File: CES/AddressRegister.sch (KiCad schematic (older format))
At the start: 8 parts

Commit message: Adding 74HC versions of 74LS chips
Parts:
- removed U?: RE1, symbol 74xx:74LS173
- removed U?: RE2, symbol 74xx:74LS173
- removed U?: RE3, symbol 74xx:74LS173
- removed U?: RE4, symbol 74xx:74LS173
- added U?: RE1, symbol CES:74HC173
- added U?: RE2, symbol CES:74HC173
- added U?: RE3, symbol CES:74HC173
- added U?: RE4, symbol CES:74HC173
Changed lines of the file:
@@
 Comment4 ""
 $EndDescr
-$Comp
-L 74xx:74LS173 U?
-U 1 1 61BF820F
-P 4050 1750
-F 0 "U?" H 4300 2500 50  0000 C CNN
-F 1 "RE1" H 4050 1750 50  0000 C CNN
-F 2 "" H 4050 1750 50  0001 C CNN
-F 3 "http://www.ti.com/lit/gpn/sn74LS173" H 4050 1750 50  0001 C CNN
-	1    4050 1750
-	1    0    0    -1
-$EndComp
-$Comp
-L 74xx:74LS173 U?
-U 1 1 61BF8215
-P 4050 4100
-F 0 "U?" H 4300 4850 50  0000 C CNN
-F 1 "RE2" H 4050 4100 50  0000 C CNN
-F 2 "" H 4050 4100 50  0001 C CNN
-F 3 "http://www.ti.com/lit/gpn/sn74LS173" H 4050 4100 50  0001 C CNN
-	1    4050 4100
-	1    0    0    -1
-$EndComp
-$Comp
-L 74xx:74LS173 U?
-U 1 1 61BF821B
-P 4050 6450
-F 0 "U?" H 4300 7200 50  0000 C CNN
-F 1 "RE3" H 4050 6450 50  0000 C CNN
-F 2 "" H 4050 6450 50  0001 C CNN
-F 3 "http://www.ti.com/lit/gpn/sn74LS173" H 4050 6450 50  0001 C CNN
-	1    4050 6450
-	1    0    0    -1
-$EndComp
-$Comp
-L 74xx:74LS173 U?
-U 1 1 61BF8221
-P 4050 8800
-F 0 "U?" H 4300 9600 50  0000 C CNN
-F 1 "RE4" H 4050 8800 50  0000 C CNN
-F 2 "" H 4050 8800 50  0001 C CNN
-F 3 "http://www.ti.com/lit/gpn/sn74LS173" H 4050 8800 50  0001 C CNN
-	1    4050 8800
-	1    0    0    -1
-$EndComp
 Wire Wire Line
 	4550 1150 5750 1150
@@
 Wire Wire Line
 	1900 10350 1750 10350
+$Comp
+L CES:74HC173 U?
+U 1 1 60900C75
+P 4050 1750
+F 0 "U?" H 4050 2831 50  0000 C CNN
+F 1 "RE1" H 4050 1750 50  0000 C CNN
+F 2 "" H 4050 1750 50  0001 C CNN
+F 3 "http://www.ti.com/lit/gpn/cd74HC173" H 4050 1750 50  0001 C CNN
+	1    4050 1750
+	1    0    0    -1
+$EndComp
+$Comp
+L CES:74HC173 U?
+U 1 1 60901D89
+P 4050 4100
+F 0 "U?" H 4050 5181 50  0000 C CNN
+F 1 "RE2" H 4050 4100 50  0000 C CNN
+F 2 "" H 4050 4100 50  0001 C CNN
+F 3 "http://www.ti.com/lit/gpn/cd74HC173" H 4050 4100 50  0001 C CNN
+	1    4050 4100
+	1    0    0    -1
+$EndComp
+$Comp
+L CES:74HC173 U?
+U 1 1 609029C7
+P 4050 6450
+F 0 "U?" H 4050 7531 50  0000 C CNN
+F 1 "RE3" H 4050 6450 50  0000 C CNN
+F 2 "" H 4050 6450 50  0001 C CNN
+F 3 "http://www.ti.com/lit/gpn/cd74HC173" H 4050 6450 50  0001 C CNN
+	1    4050 6450
+	1    0    0    -1
+$EndComp
+$Comp
+L CES:74HC173 U?
+U 1 1 609031EB
+P 4050 8800
+F 0 "U?" H 4050 9881 50  0000 C CNN
+F 1 "RE4" H 4050 8800 50  0000 C CNN
+F 2 "" H 4050 8800 50  0001 C CNN
+F 3 "http://www.ti.com/lit/gpn/cd74HC173" H 4050 8800 50  0001 C CNN
+	1    4050 8800
+	1    0    0    -1
+$EndComp
 $EndSCHEMATC

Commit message: Control Unit
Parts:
- gave numbers to parts that had none: 8
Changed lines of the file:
@@
 $Descr A4 8268 11693 portrait
 encoding utf-8
-Sheet 7 16
+Sheet 7 17
 Title "CES"
 Date "2021-04-24"
@@
 VEB13
 $Comp
-L power:GND #PWR?
+L power:GND #PWR0714
 U 1 1 60A1EDC1
 P 4050 9700
-F 0 "#PWR?" H 4050 9450 50  0001 C CNN
+F 0 "#PWR0714" H 4050 9450 50  0001 C CNN
 F 1 "GND" H 4055 9527 50  0000 C CNN
 F 2 "" H 4050 9700 50  0001 C CNN
@@
 $EndComp
 $Comp
-L power:GND #PWR?
+L power:GND #PWR0712
 U 1 1 60A1F39E
 P 4050 7350
-F 0 "#PWR?" H 4050 7100 50  0001 C CNN
+F 0 "#PWR0712" H 4050 7100 50  0001 C CNN
 F 1 "GND" H 4055 7177 50  0000 C CNN
 F 2 "" H 4050 7350 50  0001 C CNN
@@
 $EndComp
 $Comp
-L power:GND #PWR?
+L power:GND #PWR0710
 U 1 1 60A1F890
 P 4050 5000
-F 0 "#PWR?" H 4050 4750 50  0001 C CNN
+F 0 "#PWR0710" H 4050 4750 50  0001 C CNN
 F 1 "GND" H 4055 4827 50  0000 C CNN
 F 2 "" H 4050 5000 50  0001 C CNN
@@
 $EndComp
 $Comp
-L power:GND #PWR?
+L power:GND #PWR0708
 U 1 1 60A1FDC0
 P 4050 2650
-F 0 "#PWR?" H 4050 2400 50  0001 C CNN
+F 0 "#PWR0708" H 4050 2400 50  0001 C CNN
 F 1 "GND" H 4055 2477 50  0000 C CNN
 F 2 "" H 4050 2650 50  0001 C CNN
@@
 $EndComp
 $Comp
-L power:VCC #PWR?
+L power:VCC #PWR0707
 U 1 1 60A20410
 P 4050 850
-F 0 "#PWR?" H 4050 700 50  0001 C CNN
+F 0 "#PWR0707" H 4050 700 50  0001 C CNN
 F 1 "VCC" H 4065 1023 50  0000 C CNN
 F 2 "" H 4050 850 50  0001 C CNN
@@
 $EndComp
 $Comp
-L power:VCC #PWR?
+L power:VCC #PWR0709
 U 1 1 60A20A35
 P 4050 3200
-F 0 "#PWR?" H 4050 3050 50  0001 C CNN
+F 0 "#PWR0709" H 4050 3050 50  0001 C CNN
 F 1 "VCC" H 4065 3373 50  0000 C CNN
 F 2 "" H 4050 3200 50  0001 C CNN
@@
 $EndComp
 $Comp
-L power:VCC #PWR?
+L power:VCC #PWR0711
 U 1 1 60A20DA9
 P 4050 5550
-F 0 "#PWR?" H 4050 5400 50  0001 C CNN
+F 0 "#PWR0711" H 4050 5400 50  0001 C CNN
 F 1 "VCC" H 4065 5723 50  0000 C CNN
 F 2 "" H 4050 5550 50  0001 C CNN
@@
 $EndComp
 $Comp
-L power:VCC #PWR?
+L power:VCC #PWR0713
 U 1 1 60A2119F
 P 4050 7900
-F 0 "#PWR?" H 4050 7750 50  0001 C CNN
+F 0 "#PWR0713" H 4050 7750 50  0001 C CNN
 F 1 "VCC" H 4065 8073 50  0000 C CNN
 F 2 "" H 4050 7900 50  0001 C CNN
@@
 Connection ~ 3350 6650
 $Comp
-L power:GND #PWR?
+L power:GND #PWR0705
 U 1 1 60A6C19B
 P 3350 7150
-F 0 "#PWR?" H 3350 6900 50  0001 C CNN
+F 0 "#PWR0705" H 3350 6900 50  0001 C CNN
 F 1 "GND" H 3355 6977 50  0000 C CNN
 F 2 "" H 3350 7150 50  0001 C CNN
@@
 Connection ~ 3350 9000
 $Comp
-L power:GND #PWR?
+L power:GND #PWR0706
 U 1 1 60A6D091
 P 3350 9500
-F 0 "#PWR?" H 3350 9250 50  0001 C CNN
+F 0 "#PWR0706" H 3350 9250 50  0001 C CNN
 F 1 "GND" H 3355 9327 50  0000 C CNN
 F 2 "" H 3350 9500 50  0001 C CNN
@@
 Connection ~ 3350 4300
 $Comp
-L power:GND #PWR?
+L power:GND #PWR0704
 U 1 1 60A6E8ED
 P 3350 4800
-F 0 "#PWR?" H 3350 4550 50  0001 C CNN
+F 0 "#PWR0704" H 3350 4550 50  0001 C CNN
 F 1 "GND" H 3355 4627 50  0000 C CNN
 F 2 "" H 3350 4800 50  0001 C CNN
@@
 Connection ~ 3350 1950
 $Comp
-L power:GND #PWR?
+L power:GND #PWR0703
 U 1 1 60A6F961
 P 3350 2450
-F 0 "#PWR?" H 3350 2200 50  0001 C CNN
+F 0 "#PWR0703" H 3350 2200 50  0001 C CNN
 F 1 "GND" H 3355 2277 50  0000 C CNN
 F 2 "" H 3350 2450 50  0001 C CNN
@@
 	2350 8300 3550 8300
 $Comp
-L Device:C C?
+L Device:C C701
 U 1 1 60A83BCD
 P 1450 10600
-F 0 "C?" H 1500 10700 50  0000 L CNN
+F 0 "C701" H 1500 10700 50  0000 L CNN
 F 1 "100nF" H 1500 10500 50  0000 L CNN
 F 2 "" H 1488 10450 50  0001 C CNN
@@
 $EndComp
 $Comp
-L Device:C C?
+L Device:C C702
 U 1 1 60A83BD3
 P 1750 10600
-F 0 "C?" H 1800 10700 50  0000 L CNN
+F 0 "C702" H 1800 10700 50  0000 L CNN
 F 1 "100nF" H 1800 10500 50  0000 L CNN
 F 2 "" H 1788 10450 50  0001 C CNN
@@
 $EndComp
 $Comp
-L Device:C C?
+L Device:C C703
 U 1 1 60A83BD9
 P 2050 10600
-F 0 "C?" H 2100 10700 50  0000 L CNN
+F 0 "C703" H 2100 10700 50  0000 L CNN
 F 1 "100nF" H 2100 10500 50  0000 L CNN
 F 2 "" H 2088 10450 50  0001 C CNN
@@
 $EndComp
 $Comp
-L Device:C C?
+L Device:C C704
 U 1 1 60A83BDF
 P 2350 10600
-F 0 "C?" H 2400 10700 50  0000 L CNN
+F 0 "C704" H 2400 10700 50  0000 L CNN
 F 1 "100nF" H 2400 10500 50  0000 L CNN
 F 2 "" H 2388 10450 50  0001 C CNN
@@
 	1750 10850 1900 10850
 $Comp
-L power:GND #PWR?
+L power:GND #PWR0702
 U 1 1 60A83BF7
 P 1900 10850
-F 0 "#PWR?" H 1900 10600 50  0001 C CNN
+F 0 "#PWR0702" H 1900 10600 50  0001 C CNN
 F 1 "GND" H 1905 10677 50  0000 C CNN
 F 2 "" H 1900 10850 50  0001 C CNN
@@
 	1900 10850 2050 10850
 $Comp
-L power:VCC #PWR?
+L power:VCC #PWR0701
 U 1 1 60A83BFF
 P 1900 10350
-F 0 "#PWR?" H 1900 10200 50  0001 C CNN
+F 0 "#PWR0701" H 1900 10200 50  0001 C CNN
 F 1 "VCC" H 1915 10523 50  0000 C CNN
 F 2 "" H 1900 10350 50  0001 C CNN
@@
 	1900 10350 1750 10350
 $Comp
-L CES:74HC173 U?
+L CES:74HC173 U701
 U 1 1 60900C75
 P 4050 1750
-F 0 "U?" H 4050 2831 50  0000 C CNN
+F 0 "U701" H 4050 2831 50  0000 C CNN
 F 1 "RE1" H 4050 1750 50  0000 C CNN
 F 2 "" H 4050 1750 50  0001 C CNN
@@
 $EndComp
 $Comp
-L CES:74HC173 U?
+L CES:74HC173 U702
 U 1 1 60901D89
 P 4050 4100
-F 0 "U?" H 4050 5181 50  0000 C CNN
+F 0 "U702" H 4050 5181 50  0000 C CNN
 F 1 "RE2" H 4050 4100 50  0000 C CNN
 F 2 "" H 4050 4100 50  0001 C CNN
@@
 $EndComp
 $Comp
-L CES:74HC173 U?
+L CES:74HC173 U703
 U 1 1 609029C7
 P 4050 6450
-F 0 "U?" H 4050 7531 50  0000 C CNN
+F 0 "U703" H 4050 7531 50  0000 C CNN
 F 1 "RE3" H 4050 6450 50  0000 C CNN
 F 2 "" H 4050 6450 50  0001 C CNN
@@
 $EndComp
 $Comp
-L CES:74HC173 U?
+L CES:74HC173 U704
 U 1 1 609031EB
 P 4050 8800
-F 0 "U?" H 4050 9881 50  0000 C CNN
+F 0 "U704" H 4050 9881 50  0000 C CNN
 F 1 "RE4" H 4050 8800 50  0000 C CNN
 F 2 "" H 4050 8800 50  0001 C CNN

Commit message: Assigning footprints and generating netlist
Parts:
- C701, C702, C703, C704: footprint (none) -> Capacitor_THT:CP_Radial_D5.0mm_P2.50mm
- U701, U702, U703, U704: footprint (none) -> Package_DIP:DIP-16_W7.62mm
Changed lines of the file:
@@
 F 0 "C701" H 1500 10700 50  0000 L CNN
 F 1 "100nF" H 1500 10500 50  0000 L CNN
-F 2 "" H 1488 10450 50  0001 C CNN
+F 2 "Capacitor_THT:CP_Radial_D5.0mm_P2.50mm" H 1488 10450 50  0001 C CNN
 F 3 "~" H 1450 10600 50  0001 C CNN
 	1    1450 10600
@@
 F 0 "C702" H 1800 10700 50  0000 L CNN
 F 1 "100nF" H 1800 10500 50  0000 L CNN
-F 2 "" H 1788 10450 50  0001 C CNN
+F 2 "Capacitor_THT:CP_Radial_D5.0mm_P2.50mm" H 1788 10450 50  0001 C CNN
 F 3 "~" H 1750 10600 50  0001 C CNN
 	1    1750 10600
@@
 F 0 "C703" H 2100 10700 50  0000 L CNN
 F 1 "100nF" H 2100 10500 50  0000 L CNN
-F 2 "" H 2088 10450 50  0001 C CNN
+F 2 "Capacitor_THT:CP_Radial_D5.0mm_P2.50mm" H 2088 10450 50  0001 C CNN
 F 3 "~" H 2050 10600 50  0001 C CNN
 	1    2050 10600
@@
 F 0 "C704" H 2400 10700 50  0000 L CNN
 F 1 "100nF" H 2400 10500 50  0000 L CNN
-F 2 "" H 2388 10450 50  0001 C CNN
+F 2 "Capacitor_THT:CP_Radial_D5.0mm_P2.50mm" H 2388 10450 50  0001 C CNN
 F 3 "~" H 2350 10600 50  0001 C CNN
 	1    2350 10600
@@
 F 0 "U701" H 4050 2831 50  0000 C CNN
 F 1 "RE1" H 4050 1750 50  0000 C CNN
-F 2 "" H 4050 1750 50  0001 C CNN
+F 2 "Package_DIP:DIP-16_W7.62mm" H 4050 1750 50  0001 C CNN
 F 3 "http://www.ti.com/lit/gpn/cd74HC173" H 4050 1750 50  0001 C CNN
 	1    4050 1750
@@
 F 0 "U702" H 4050 5181 50  0000 C CNN
 F 1 "RE2" H 4050 4100 50  0000 C CNN
-F 2 "" H 4050 4100 50  0001 C CNN
+F 2 "Package_DIP:DIP-16_W7.62mm" H 4050 4100 50  0001 C CNN
 F 3 "http://www.ti.com/lit/gpn/cd74HC173" H 4050 4100 50  0001 C CNN
 	1    4050 4100
@@
 F 0 "U703" H 4050 7531 50  0000 C CNN
 F 1 "RE3" H 4050 6450 50  0000 C CNN
-F 2 "" H 4050 6450 50  0001 C CNN
+F 2 "Package_DIP:DIP-16_W7.62mm" H 4050 6450 50  0001 C CNN
 F 3 "http://www.ti.com/lit/gpn/cd74HC173" H 4050 6450 50  0001 C CNN
 	1    4050 6450
@@
 F 0 "U704" H 4050 9881 50  0000 C CNN
 F 1 "RE4" H 4050 8800 50  0000 C CNN
-F 2 "" H 4050 8800 50  0001 C CNN
+F 2 "Package_DIP:DIP-16_W7.62mm" H 4050 8800 50  0001 C CNN
 F 3 "http://www.ti.com/lit/gpn/cd74HC173" H 4050 8800 50  0001 C CNN
 	1    4050 8800

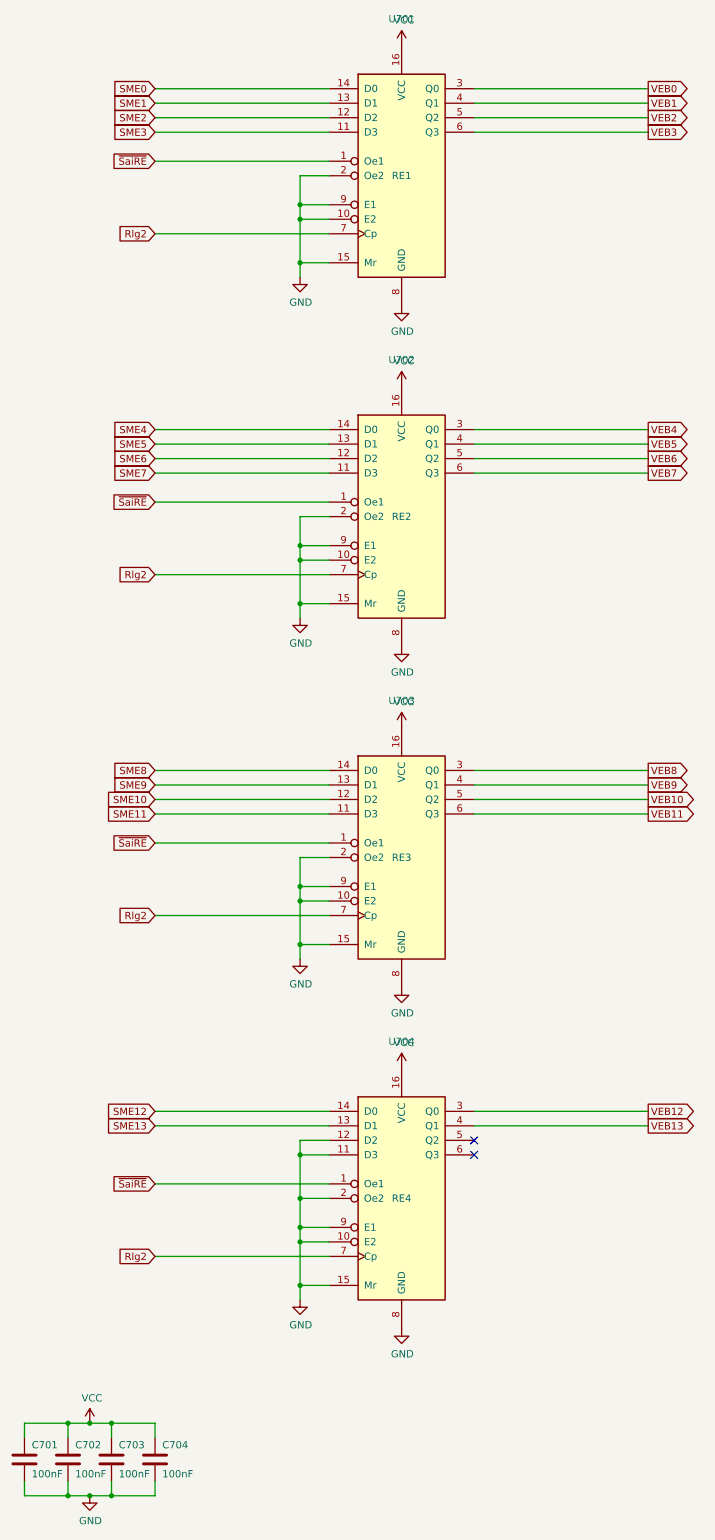
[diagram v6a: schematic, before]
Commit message: Correcting footprints errors
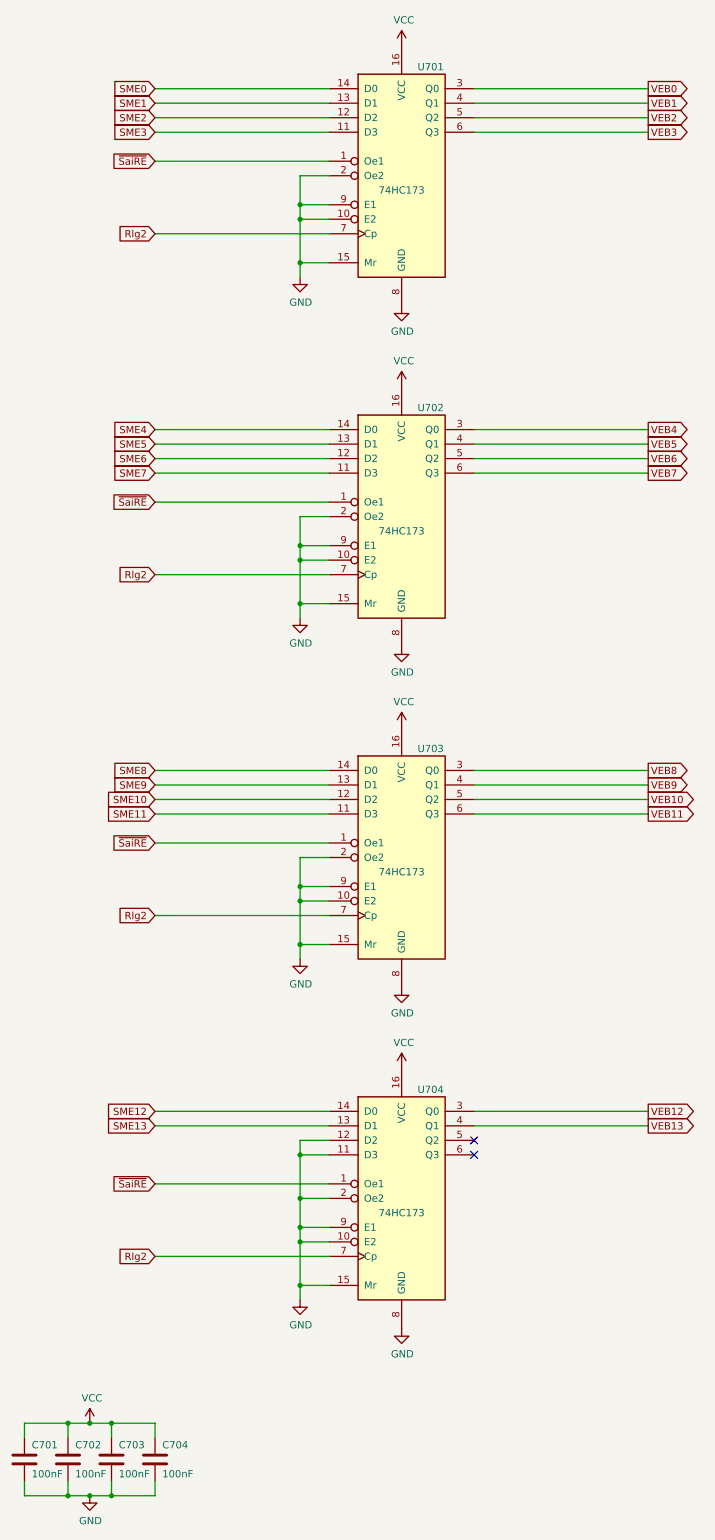
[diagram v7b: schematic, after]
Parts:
- C701, C702, C703, C704: footprint Capacitor_THT:CP_Radial_D5.0mm_P2.50mm -> Capacitor_THT:C_Disc_D4.3mm_W1.9mm_P5.00mm
- U701: value RE1 -> 74HC173
- U702: value RE2 -> 74HC173
- U703: value RE3 -> 74HC173
- U704: value RE4 -> 74HC173
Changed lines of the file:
@@
 F 0 "C701" H 1500 10700 50  0000 L CNN
 F 1 "100nF" H 1500 10500 50  0000 L CNN
-F 2 "Capacitor_THT:CP_Radial_D5.0mm_P2.50mm" H 1488 10450 50  0001 C CNN
+F 2 "Capacitor_THT:C_Disc_D4.3mm_W1.9mm_P5.00mm" H 1488 10450 50  0001 C CNN
 F 3 "~" H 1450 10600 50  0001 C CNN
 	1    1450 10600
@@
 F 0 "C702" H 1800 10700 50  0000 L CNN
 F 1 "100nF" H 1800 10500 50  0000 L CNN
-F 2 "Capacitor_THT:CP_Radial_D5.0mm_P2.50mm" H 1788 10450 50  0001 C CNN
+F 2 "Capacitor_THT:C_Disc_D4.3mm_W1.9mm_P5.00mm" H 1788 10450 50  0001 C CNN
 F 3 "~" H 1750 10600 50  0001 C CNN
 	1    1750 10600
@@
 F 0 "C703" H 2100 10700 50  0000 L CNN
 F 1 "100nF" H 2100 10500 50  0000 L CNN
-F 2 "Capacitor_THT:CP_Radial_D5.0mm_P2.50mm" H 2088 10450 50  0001 C CNN
+F 2 "Capacitor_THT:C_Disc_D4.3mm_W1.9mm_P5.00mm" H 2088 10450 50  0001 C CNN
 F 3 "~" H 2050 10600 50  0001 C CNN
 	1    2050 10600
@@
 F 0 "C704" H 2400 10700 50  0000 L CNN
 F 1 "100nF" H 2400 10500 50  0000 L CNN
-F 2 "Capacitor_THT:CP_Radial_D5.0mm_P2.50mm" H 2388 10450 50  0001 C CNN
+F 2 "Capacitor_THT:C_Disc_D4.3mm_W1.9mm_P5.00mm" H 2388 10450 50  0001 C CNN
 F 3 "~" H 2350 10600 50  0001 C CNN
 	1    2350 10600
@@
 U 1 1 60900C75
 P 4050 1750
-F 0 "U701" H 4050 2831 50  0000 C CNN
-F 1 "RE1" H 4050 1750 50  0000 C CNN
+F 0 "U701" H 4250 2500 50  0000 C CNN
+F 1 "74HC173" H 4050 1650 50  0000 C CNN
 F 2 "Package_DIP:DIP-16_W7.62mm" H 4050 1750 50  0001 C CNN
 F 3 "http://www.ti.com/lit/gpn/cd74HC173" H 4050 1750 50  0001 C CNN
@@
 U 1 1 60901D89
 P 4050 4100
-F 0 "U702" H 4050 5181 50  0000 C CNN
-F 1 "RE2" H 4050 4100 50  0000 C CNN
+F 0 "U702" H 4250 4850 50  0000 C CNN
+F 1 "74HC173" H 4050 4000 50  0000 C CNN
 F 2 "Package_DIP:DIP-16_W7.62mm" H 4050 4100 50  0001 C CNN
 F 3 "http://www.ti.com/lit/gpn/cd74HC173" H 4050 4100 50  0001 C CNN
@@
 U 1 1 609029C7
 P 4050 6450
-F 0 "U703" H 4050 7531 50  0000 C CNN
-F 1 "RE3" H 4050 6450 50  0000 C CNN
+F 0 "U703" H 4250 7200 50  0000 C CNN
+F 1 "74HC173" H 4050 6350 50  0000 C CNN
 F 2 "Package_DIP:DIP-16_W7.62mm" H 4050 6450 50  0001 C CNN
 F 3 "http://www.ti.com/lit/gpn/cd74HC173" H 4050 6450 50  0001 C CNN
@@
 U 1 1 609031EB
 P 4050 8800
-F 0 "U704" H 4050 9881 50  0000 C CNN
-F 1 "RE4" H 4050 8800 50  0000 C CNN
+F 0 "U704" H 4250 9550 50  0000 C CNN
+F 1 "74HC173" H 4050 8700 50  0000 C CNN
 F 2 "Package_DIP:DIP-16_W7.62mm" H 4050 8800 50  0001 C CNN
 F 3 "http://www.ti.com/lit/gpn/cd74HC173" H 4050 8800 50  0001 C CNN
